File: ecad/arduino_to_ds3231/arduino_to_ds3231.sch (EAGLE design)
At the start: 2 parts

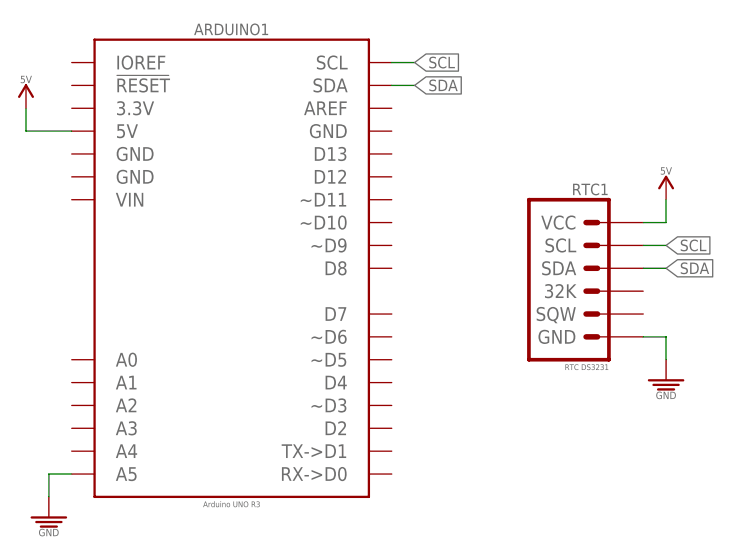
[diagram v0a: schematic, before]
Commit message: Changed 5V to 3.3V in arduino to ds3231.
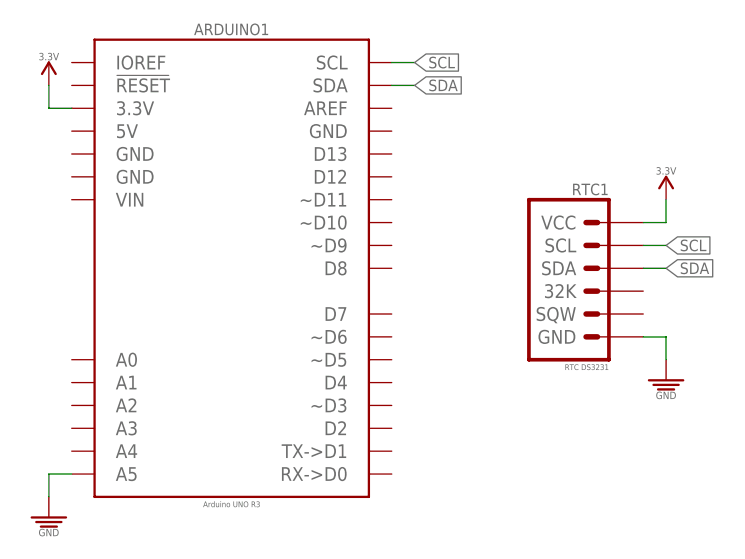
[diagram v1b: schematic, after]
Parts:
- RTC1: device PiB:RTC_DS3231_PTH_VERT-FEMALE_2.54MM -> PiB:DS3231_RTC_PTH_VERT-FEMALE_2.54MM
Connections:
- removed net 5V: ARDUINO1.5V, RTC1.VCC
- new net 3.3V: ARDUINO1.3.3V, RTC1.VCC
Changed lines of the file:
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@@
 <setting verticaltext="up"/>
 </settings>
-<grid distance="0.1" unitdist="inch" unit="inch" style="lines" multiple="1" display="yes" altdistance="0.01" altunitdist="inch" altunit="inch"/>
+<grid distance="0.1" unitdist="inch" unit="inch" style="lines" multiple="1" display="no" altdistance="0.01" altunitdist="inch" altunit="inch"/>
 <layers>
 <layer number="1" name="Top" color="4" fill="1" visible="no" active="no"/>
@@
 <parts>
 <part name="ARDUINO1" library="PiB_boards" deviceset="ARDUINO_UNO_R3_NO-HOLES_NO-AVR-ISP" device="" value="Arduino UNO R3"/>
-<part name="SUPPLY1" library="PiB_power_symbols" deviceset="5V" device=""/>
-<part name="SUPPLY2" library="PiB_power_symbols" deviceset="5V" device=""/>
 <part name="SUPPLY3" library="PiB_power_symbols" deviceset="GND" device=""/>
 <part name="SUPPLY4" library="PiB_power_symbols" deviceset="GND" device=""/>
-<part name="RTC1" library="PiB" deviceset="RTC_DS3231" device="_PTH_VERT-FEMALE_2.54MM" package3d_urn="urn:adsk.eagle:package:4270212/2" value="RTC DS3231"/>
+<part name="SUPPLY1" library="PiB_power_symbols" deviceset="3.3V" device=""/>
+<part name="SUPPLY2" library="PiB_power_symbols" deviceset="3.3V" device=""/>
+<part name="RTC1" library="PiB" deviceset="DS3231_RTC" device="_PTH_VERT-FEMALE_2.54MM" package3d_urn="urn:adsk.eagle:package:4270212/2" value="RTC DS3231"/>
 </parts>
 <sheets>
@@
 <attribute name="VALUE" x="40.64" y="17.272" size="0.635" layer="96" font="vector" ratio="10" align="top-center"/>
 </instance>
-<instance part="SUPPLY1" gate="5V" x="17.78" y="60.96" smashed="yes"/>
-<instance part="SUPPLY2" gate="5V" x="88.9" y="50.8" smashed="yes"/>
 <instance part="SUPPLY3" gate="GND" x="88.9" y="30.48" smashed="yes"/>
 <instance part="SUPPLY4" gate="GND" x="20.32" y="15.24" smashed="yes"/>
+<instance part="SUPPLY1" gate="3.3V" x="88.9" y="50.8" smashed="yes"/>
+<instance part="SUPPLY2" gate="3.3V" x="20.32" y="63.5" smashed="yes"/>
 <instance part="RTC1" gate="G$1" x="81.28" y="43.18" smashed="yes">
 <attribute name="NAME" x="82.55" y="51.308" size="1.27" layer="95" font="vector" ratio="10" align="bottom-right"/>
@@
 </busses>
 <nets>
-<net name="5V" class="0">
-<segment>
-<wire x1="17.78" y1="60.96" x2="17.78" y2="58.42" width="0.1524" layer="91"/>
-<pinref part="ARDUINO1" gate="G$1" pin="5V"/>
-<wire x1="17.78" y1="58.42" x2="22.86" y2="58.42" width="0.1524" layer="91"/>
-<pinref part="SUPPLY1" gate="5V" pin="5V"/>
-</segment>
-<segment>
-<pinref part="RTC1" gate="G$1" pin="VCC"/>
-<wire x1="86.36" y1="48.26" x2="88.9" y2="48.26" width="0.1524" layer="91"/>
-<pinref part="SUPPLY2" gate="5V" pin="5V"/>
-<wire x1="88.9" y1="48.26" x2="88.9" y2="50.8" width="0.1524" layer="91"/>
-</segment>
-</net>
 <net name="GND" class="0">
 <segment>
@@
 </segment>
 <segment>
-<pinref part="RTC1" gate="G$1" pin="GND"/>
 <wire x1="86.36" y1="35.56" x2="88.9" y2="35.56" width="0.1524" layer="91"/>
 <pinref part="SUPPLY3" gate="GND" pin="GND"/>
 <wire x1="88.9" y1="35.56" x2="88.9" y2="33.02" width="0.1524" layer="91"/>
+<pinref part="RTC1" gate="G$1" pin="GND"/>
 </segment>
 </net>
 <net name="SDA" class="0">
 <segment>
-<pinref part="RTC1" gate="G$1" pin="SDA"/>
 <wire x1="88.9" y1="43.18" x2="86.36" y2="43.18" width="0.1524" layer="91"/>
 <label x="88.9" y="43.18" size="1.27" layer="95" font="vector" ratio="10" xref="yes"/>
+<pinref part="RTC1" gate="G$1" pin="SDA"/>
 </segment>
 <segment>
@@
 </segment>
 <segment>
-<pinref part="RTC1" gate="G$1" pin="SCL"/>
 <wire x1="88.9" y1="45.72" x2="86.36" y2="45.72" width="0.1524" layer="91"/>
 <label x="88.9" y="45.72" size="1.27" layer="95" font="vector" ratio="10" xref="yes"/>
-</segment>
-</net>
+<pinref part="RTC1" gate="G$1" pin="SCL"/>
+</segment>
+</net>
+<net name="3.3V" class="0">
+<segment>
+<pinref part="SUPPLY2" gate="3.3V" pin="3.3V"/>
+<pinref part="ARDUINO1" gate="G$1" pin="3.3V"/>
+<wire x1="20.32" y1="63.5" x2="20.32" y2="60.96" width="0.1524" layer="91"/>
+<wire x1="20.32" y1="60.96" x2="22.86" y2="60.96" width="0.1524" layer="91"/>
+</segment>
+<segment>
+<pinref part="SUPPLY1" gate="3.3V" pin="3.3V"/>
+<wire x1="86.36" y1="48.26" x2="88.9" y2="48.26" width="0.1524" layer="91"/>
+<wire x1="88.9" y1="48.26" x2="88.9" y2="50.8" width="0.1524" layer="91"/>
+<pinref part="RTC1" gate="G$1" pin="VCC"/>
+</segment>
+</net>
